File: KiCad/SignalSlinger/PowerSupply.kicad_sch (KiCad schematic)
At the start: 44 parts, among them J201 Barrel_Jack_Switch, J203 External Fan Power, J204 Controlled Power, U201 LP2985-3.3, U202 LP2985-3.3, U203 TPS63060, U204 TPS22810DBVT, U205 uA7805

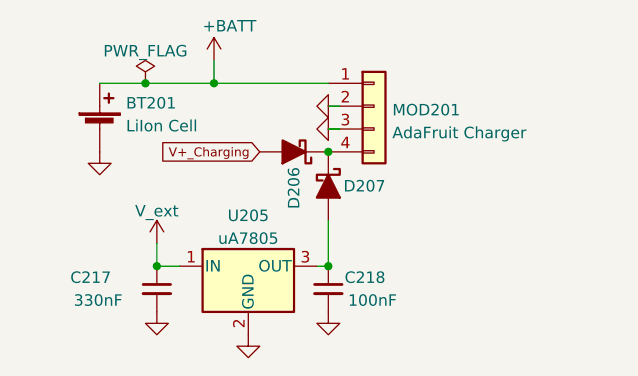
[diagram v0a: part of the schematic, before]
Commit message: Rev 2.3
Updates from initial PCB build.
Added thermal fuse F101
Support for regulated voltage
Support for charging LiPo via transmitter external power source
Updated BOM
Updated PCB and schematic
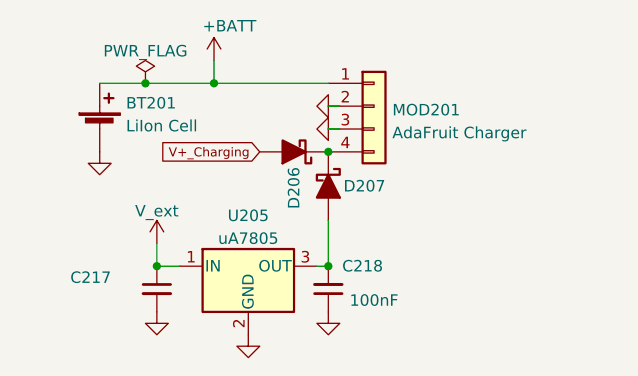
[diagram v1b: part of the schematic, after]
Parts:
- C217: value 330nF -> (none); footprint Capacitor_SMD:C_0805_2012Metric -> (none); Digi-Key Part No. 399-C0805C103J5GEC7800CT-ND -> 478-9924-1-ND; LCSC Part Number C3887673 -> C342818; Link https://www.digikey.com/short/qd893213 -> https://www.digikey.com/products/en?keywords=478-9924-1-ND; Manufacturer KEMET -> AVX Corporation; Manufacturer PN C0805C103J5GEC7800 -> 08051C474K4Z2A
- C218: Digi-Key Part No. 399-C0805C103J5GEC7800CT-ND -> 1276-1099-1-ND; LCSC Part Number C3887673 -> C29926; Link https://www.digikey.com/short/qd893213 -> https://www.digikey.com/short/q2f22qnq; Manufacturer KEMET -> Samsung Electro-Mechanics; Manufacturer PN C0805C103J5GEC7800 -> CL21B104KACNNNC
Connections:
- net GND: now also C218.1; no longer C218.2
- net at D207.2 (A), U205.3 (OUT): now also C218.2; no longer C218.1
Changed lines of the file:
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@@
   (title_block
     (title "SignalSlinger")
-    (date "2023-12-10")
-    (rev "2.2")
+    (date "2024-04-13")
+    (rev "2.3")
   )
   (junction (at 187.96 116.84) (diameter 0) (color 0 0 0 0)
@@
   (junction (at 189.23 41.91) (diameter 0) (color 0 0 0 0)
   )
+  (junction (at 55.88 170.18) (diameter 0) (color 0 0 0 0)
+  )
   (junction (at 229.87 41.91) (diameter 0) (color 0 0 0 0)
   )
@@
   )
   (junction (at 217.17 41.91) (diameter 0) (color 0 0 0 0)
-  )
-  (junction (at 55.88 170.18) (diameter 0) (color 0 0 0 0)
   )
   (junction (at 190.5 116.84) (diameter 0) (color 0 0 0 0)
@@
   (symbol (lib_id "power:+VSW") (at 107.95 46.99 0) (mirror y) (unit 1)
     (in_bom yes) (on_board yes)
-    (property "Reference" "#PWR?" (id 0) (at 107.95 50.8 0)
+    (property "Reference" "#PWR0153" (id 0) (at 107.95 50.8 0)
       (effects (font (size 1.27 1.27)) hide)
     )
@@
       (effects (font (size 1.27 1.27)) (justify left))
     )
-    (property "Value" "330nF" (id 1) (at 33.02 173.99 0)
-      (effects (font (size 1.27 1.27)) (justify left))
-    )
-    (property "Footprint" "Capacitor_SMD:C_0805_2012Metric" (id 2) (at 36.83 172.72 0)
+    (property "Value" "" (id 1) (at 33.02 173.99 0)
+      (effects (font (size 1.27 1.27)) (justify left))
+    )
+    (property "Footprint" "" (id 2) (at 36.83 172.72 0)
       (effects (font (size 1.27 1.27)) hide)
     )
@@
       (effects (font (size 1.27 1.27)) hide)
     )
-    (property "Digi-Key Part No." "399-C0805C103J5GEC7800CT-ND" (id 4) (at 36.83 172.72 0)
-      (effects (font (size 1.27 1.27)) hide)
-    )
-    (property "Manufacturer" "KEMET" (id 5) (at 36.83 172.72 0)
-      (effects (font (size 1.27 1.27)) hide)
-    )
-    (property "Manufacturer PN" "C0805C103J5GEC7800" (id 6) (at 36.83 172.72 0)
-      (effects (font (size 1.27 1.27)) hide)
-    )
-    (property "Description" "CAP CER 0805 10NF 50V C0G 5%" (id 7) (at 36.83 172.72 0)
-      (effects (font (size 1.27 1.27)) hide)
-    )
-    (property "Link" "https://www.digikey.com/short/qd893213" (id 8) (at 36.83 172.72 0)
-      (effects (font (size 1.27 1.27)) hide)
-    )
-    (property "LCSC Part Number" "C3887673" (id 9) (at 36.83 172.72 0)
+    (property "Digi-Key Part No." "478-9924-1-ND" (id 4) (at 36.83 172.72 0)
+      (effects (font (size 1.27 1.27)) hide)
+    )
+    (property "Manufacturer" "AVX Corporation" (id 5) (at 36.83 172.72 0)
+      (effects (font (size 1.27 1.27)) hide)
+    )
+    (property "Manufacturer PN" "08051C474K4Z2A" (id 6) (at 36.83 172.72 0)
+      (effects (font (size 1.27 1.27)) hide)
+    )
+    (property "Description" "CAP CER 0.47UF 100V X7R 0805" (id 7) (at 36.83 172.72 0)
+      (effects (font (size 1.27 1.27)) hide)
+    )
+    (property "Link" "https://www.digikey.com/products/en?keywords=478-9924-1-ND" (id 8) (at 36.83 172.72 0)
+      (effects (font (size 1.27 1.27)) hide)
+    )
+    (property "LCSC Part Number" "C342818" (id 9) (at 36.83 172.72 0)
       (effects (font (size 1.27 1.27)) hide)
     )
@@
     (pin "2")
   )
+  (symbol (lib_id "Device:C_Small") (at 55.88 172.72 180) (unit 1)
+    (in_bom yes) (on_board yes)
+    (property "Reference" "C218" (id 0) (at 59.69 170.18 0))
+    (property "Value" "100nF" (id 1) (at 60.96 173.99 0))
+    (property "Footprint" "Capacitor_SMD:C_0805_2012Metric" (id 2) (at 55.88 172.72 0)
+      (effects (font (size 1.27 1.27)) hide)
+    )
+    (property "Datasheet" "" (id 3) (at 55.88 172.72 0)
+      (effects (font (size 1.27 1.27)) hide)
+    )
+    (property "Digi-Key Part No." "1276-1099-1-ND" (id 4) (at 55.88 172.72 0)
+      (effects (font (size 1.27 1.27)) hide)
+    )
+    (property "Manufacturer" "Samsung Electro-Mechanics" (id 5) (at 55.88 172.72 0)
+      (effects (font (size 1.27 1.27)) hide)
+    )
+    (property "Manufacturer PN" "CL21B104KACNNNC" (id 6) (at 55.88 172.72 0)
+      (effects (font (size 1.27 1.27)) hide)
+    )
+    (property "Description" "CAP CER 0.1UF 25V X7R 0805" (id 7) (at 55.88 172.72 0)
+      (effects (font (size 1.27 1.27)) hide)
+    )
+    (property "Link" "https://www.digikey.com/short/q2f22qnq" (id 8) (at 55.88 172.72 0)
+      (effects (font (size 1.27 1.27)) hide)
+    )
+    (property "LCSC Part Number" "C29926" (id 9) (at 55.88 172.72 0)
+      (effects (font (size 1.27 1.27)) hide)
+    )
+    (pin "1")
+    (pin "2")
+  )
   (symbol (lib_id "power:GND") (at 226.06 119.38 0) (unit 1)
     (in_bom yes) (on_board yes) (fields_autoplaced)
@@
       (effects (font (size 1.27 1.27)) hide)
     )
-    (pin "1")
-    (pin "2")
-  )
-  (symbol (lib_id "Device:C_Small") (at 55.88 172.72 0) (mirror y) (unit 1)
-    (in_bom yes) (on_board yes)
-    (property "Reference" "C218" (id 0) (at 62.23 171.45 0)
-      (effects (font (size 1.27 1.27)) (justify left))
-    )
-    (property "Value" "100nF" (id 1) (at 63.5 173.99 0)
-      (effects (font (size 1.27 1.27)) (justify left))
-    )
-    (property "Footprint" "Capacitor_SMD:C_0805_2012Metric" (id 2) (at 55.88 172.72 0)
-      (effects (font (size 1.27 1.27)) hide)
-    )
-    (property "Datasheet" "" (id 3) (at 55.88 172.72 0)
-      (effects (font (size 1.27 1.27)) hide)
-    )
-    (property "Digi-Key Part No." "399-C0805C103J5GEC7800CT-ND" (id 4) (at 55.88 172.72 0)
-      (effects (font (size 1.27 1.27)) hide)
-    )
-    (property "Manufacturer" "KEMET" (id 5) (at 55.88 172.72 0)
-      (effects (font (size 1.27 1.27)) hide)
-    )
-    (property "Manufacturer PN" "C0805C103J5GEC7800" (id 6) (at 55.88 172.72 0)
-      (effects (font (size 1.27 1.27)) hide)
-    )
-    (property "Description" "CAP CER 0805 10NF 50V C0G 5%" (id 7) (at 55.88 172.72 0)
-      (effects (font (size 1.27 1.27)) hide)
-    )
-    (property "Link" "https://www.digikey.com/short/qd893213" (id 8) (at 55.88 172.72 0)
-      (effects (font (size 1.27 1.27)) hide)
-    )
-    (property "LCSC Part Number" "C3887673" (id 9) (at 55.88 172.72 0)
-      (effects (font (size 1.27 1.27)) hide)
-    )

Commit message: Ver 2.3
Updates to BOM information.
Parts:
- C213, C214, C215: value 22uF -> (none); footprint Capacitor_SMD:C_0805_2012Metric -> (none); Digi-Key Part No. 1276-3373-1-ND -> 1276-6780-1-ND; LCSC Part Number C337455 -> (none); Link https://www.digikey.com/products/en?keywords=1276-3373-1-ND -> (none); Manufacturer PN CL32A226MAJNNNE -> CL21A226MOCLRNC
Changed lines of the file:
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@@
     (pin "3")
-  )
-  (symbol (lib_id "Device:C_Small") (at 203.2 63.5 180) (unit 1)
-    (in_bom yes) (on_board yes)
-    (property "Reference" "C213" (id 0) (at 210.82 62.23 0)
-      (effects (font (size 1.27 1.27)) (justify left))
-    )
-    (property "Value" "22uF" (id 1) (at 210.82 64.77 0)
-      (effects (font (size 1.27 1.27)) (justify left))
-    )
-    (property "Footprint" "Capacitor_SMD:C_0805_2012Metric" (id 2) (at 203.2 63.5 0)
-      (effects (font (size 1.27 1.27)) hide)
-    )
-    (property "Datasheet" "" (id 3) (at 203.2 63.5 0)
-      (effects (font (size 1.27 1.27)) hide)
-    )
-    (property "Digi-Key Part No." "1276-3373-1-ND" (id 4) (at 203.2 63.5 0)
-      (effects (font (size 1.27 1.27)) hide)
-    )
-    (property "Link" "https://www.digikey.com/products/en?keywords=1276-3373-1-ND" (id 5) (at 203.2 63.5 0)
-      (effects (font (size 1.524 1.524)) hide)
-    )
-    (property "Manufacturer" "Samsung Electro-Mechanics" (id 6) (at 203.2 63.5 90)
-      (effects (font (size 1.27 1.27)) hide)
-    )
-    (property "Manufacturer PN" "CL32A226MAJNNNE" (id 7) (at 203.2 63.5 90)
-      (effects (font (size 1.27 1.27)) hide)
-    )
-    (property "Description" "CAP CER 22UF 25V X5R 1210" (id 8) (at 203.2 63.5 90)
-      (effects (font (size 1.27 1.27)) hide)
-    )
-    (property "LCSC Part Number" "C337455" (id 9) (at 203.2 63.5 0)
-      (effects (font (size 1.27 1.27)) hide)
-    )
-    (pin "1")
-    (pin "2")
   )
   (symbol (lib_id "power:V_ext") (at 71.12 96.52 0) (unit 1)
@@
     (pin "1")
   )
+  (symbol (lib_id "Device:C_Small") (at 203.2 63.5 180) (unit 1)
+    (in_bom yes) (on_board yes)
+    (property "Reference" "C213" (id 0) (at 210.82 62.23 0)
+      (effects (font (size 1.27 1.27)) (justify left))
+    )
+    (property "Value" "" (id 1) (at 210.82 64.77 0)
+      (effects (font (size 1.27 1.27)) (justify left))
+    )
+    (property "Footprint" "" (id 2) (at 203.2 63.5 0)
+      (effects (font (size 1.27 1.27)) hide)
+    )
+    (property "Datasheet" "" (id 3) (at 203.2 63.5 0)
+      (effects (font (size 1.27 1.27)) hide)
+    )
+    (property "Digi-Key Part No." "1276-6780-1-ND" (id 4) (at 203.2 63.5 0)
+      (effects (font (size 1.27 1.27)) hide)
+    )
+    (property "Manufacturer" "Samsung Electro-Mechanics" (id 6) (at 203.2 63.5 90)
+      (effects (font (size 1.27 1.27)) hide)
+    )
+    (property "Manufacturer PN" "CL21A226MOCLRNC" (id 7) (at 203.2 63.5 90)
+      (effects (font (size 1.27 1.27)) hide)
+    )
+    (property "Description" "CAP CER 22UF 16V X5R 0805" (id 8) (at 203.2 63.5 90)
+      (effects (font (size 1.27 1.27)) hide)
+    )
+    (pin "1")
+    (pin "2")
+  )
   (symbol (lib_id "Device:C_Small") (at 229.87 63.5 180) (unit 1)
     (in_bom yes) (on_board yes)
@@
       (effects (font (size 1.27 1.27)) (justify left))
     )
-    (property "Value" "22uF" (id 1) (at 237.49 64.77 0)
-      (effects (font (size 1.27 1.27)) (justify left))
-    )
-    (property "Footprint" "Capacitor_SMD:C_0805_2012Metric" (id 2) (at 229.87 63.5 0)
+    (property "Value" "" (id 1) (at 237.49 64.77 0)
+      (effects (font (size 1.27 1.27)) (justify left))
+    )
+    (property "Footprint" "" (id 2) (at 229.87 63.5 0)
       (effects (font (size 1.27 1.27)) hide)
     )
@@
       (effects (font (size 1.27 1.27)) hide)
     )
-    (property "Digi-Key Part No." "1276-3373-1-ND" (id 4) (at 229.87 63.5 0)
-      (effects (font (size 1.27 1.27)) hide)
-    )
-    (property "Link" "https://www.digikey.com/products/en?keywords=1276-3373-1-ND" (id 5) (at 229.87 63.5 0)
-      (effects (font (size 1.524 1.524)) hide)
+    (property "Digi-Key Part No." "1276-6780-1-ND" (id 4) (at 229.87 63.5 0)
+      (effects (font (size 1.27 1.27)) hide)
     )
     (property "Manufacturer" "Samsung Electro-Mechanics" (id 6) (at 229.87 63.5 90)
       (effects (font (size 1.27 1.27)) hide)
     )
-    (property "Manufacturer PN" "CL32A226MAJNNNE" (id 7) (at 229.87 63.5 90)
-      (effects (font (size 1.27 1.27)) hide)
-    )
-    (property "Description" "CAP CER 22UF 25V X5R 1210" (id 8) (at 229.87 63.5 90)
-      (effects (font (size 1.27 1.27)) hide)
-    )
-    (property "LCSC Part Number" "C337455" (id 9) (at 229.87 63.5 0)
+    (property "Manufacturer PN" "CL21A226MOCLRNC" (id 7) (at 229.87 63.5 90)
+      (effects (font (size 1.27 1.27)) hide)
+    )
+    (property "Description" "CAP CER 22UF 16V X5R 0805" (id 8) (at 229.87 63.5 90)
       (effects (font (size 1.27 1.27)) hide)
     )
@@
     )
     (property "LCSC Part Number" "C3887673" (id 9) (at 31.75 121.92 0)
+      (effects (font (size 1.27 1.27)) hide)
+    )
+    (pin "1")
+    (pin "2")
+  )
+  (symbol (lib_id "Device:C_Small") (at 217.17 63.5 180) (unit 1)
+    (in_bom yes) (on_board yes)
+    (property "Reference" "C214" (id 0) (at 224.79 62.23 0)
+      (effects (font (size 1.27 1.27)) (justify left))
+    )
+    (property "Value" "" (id 1) (at 224.79 64.77 0)
+      (effects (font (size 1.27 1.27)) (justify left))
+    )
+    (property "Footprint" "" (id 2) (at 217.17 63.5 0)
+      (effects (font (size 1.27 1.27)) hide)
+    )
+    (property "Datasheet" "" (id 3) (at 217.17 63.5 0)
+      (effects (font (size 1.27 1.27)) hide)
+    )
+    (property "Digi-Key Part No." "1276-6780-1-ND" (id 4) (at 217.17 63.5 0)
+      (effects (font (size 1.27 1.27)) hide)
+    )
+    (property "Manufacturer" "Samsung Electro-Mechanics" (id 6) (at 217.17 63.5 90)
+      (effects (font (size 1.27 1.27)) hide)
+    )
+    (property "Manufacturer PN" "CL21A226MOCLRNC" (id 7) (at 217.17 63.5 90)
+      (effects (font (size 1.27 1.27)) hide)
+    )
+    (property "Description" "CAP CER 22UF 16V X5R 0805" (id 8) (at 217.17 63.5 90)
       (effects (font (size 1.27 1.27)) hide)
     )
@@
     (pin "9")
   )
-  (symbol (lib_id "Device:C_Small") (at 217.17 63.5 180) (unit 1)
-    (in_bom yes) (on_board yes)
-    (property "Reference" "C214" (id 0) (at 224.79 62.23 0)
-      (effects (font (size 1.27 1.27)) (justify left))
-    )
-    (property "Value" "22uF" (id 1) (at 224.79 64.77 0)
-      (effects (font (size 1.27 1.27)) (justify left))
-    )
-    (property "Footprint" "Capacitor_SMD:C_0805_2012Metric" (id 2) (at 217.17 63.5 0)
-      (effects (font (size 1.27 1.27)) hide)
-    )
-    (property "Datasheet" "" (id 3) (at 217.17 63.5 0)
-      (effects (font (size 1.27 1.27)) hide)
-    )
-    (property "Digi-Key Part No." "1276-3373-1-ND" (id 4) (at 217.17 63.5 0)
-      (effects (font (size 1.27 1.27)) hide)
-    )
-    (property "Link" "https://www.digikey.com/products/en?keywords=1276-3373-1-ND" (id 5) (at 217.17 63.5 0)
-      (effects (font (size 1.524 1.524)) hide)
-    )
-    (property "Manufacturer" "Samsung Electro-Mechanics" (id 6) (at 217.17 63.5 90)
-      (effects (font (size 1.27 1.27)) hide)
-    )
-    (property "Manufacturer PN" "CL32A226MAJNNNE" (id 7) (at 217.17 63.5 90)
-      (effects (font (size 1.27 1.27)) hide)
-    )
-    (property "Description" "CAP CER 22UF 25V X5R 1210" (id 8) (at 217.17 63.5 90)
-      (effects (font (size 1.27 1.27)) hide)
-    )
-    (property "LCSC Part Number" "C337455" (id 9) (at 217.17 63.5 0)
-      (effects (font (size 1.27 1.27)) hide)
-    )
-    (pin "1")
-    (pin "2")
-  )
   (symbol (lib_id "Regulator_Linear:LP2985-3.3") (at 44.45 118.11 0) (mirror y) (unit 1)

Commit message: Ver 2.4
Minor schematic update.
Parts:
- C213, C214, C215: value (none) -> 22uF; footprint (none) -> Capacitor_SMD:C_0805_2012Metric
- C217: value (none) -> 470nF; footprint (none) -> Capacitor_SMD:C_0805_2012Metric
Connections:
- net GND: now also C218.2; no longer C218.1
- net at D207.2 (A), U205.3 (OUT): now also C218.1; no longer C218.2
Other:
- moved on the sheet: C218
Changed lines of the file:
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@@
   (title_block
     (title "SignalSlinger")
-    (date "2024-04-13")
-    (rev "2.3")
+    (date "2024-04-15")
+    (rev "2.4")
   )
   (junction (at 187.96 116.84) (diameter 0) (color 0 0 0 0)
@@
   (junction (at 189.23 41.91) (diameter 0) (color 0 0 0 0)
   )
+  (junction (at 229.87 41.91) (diameter 0) (color 0 0 0 0)
+  )
+  (junction (at 73.66 109.22) (diameter 0) (color 0 0 0 0)
+  )
+  (junction (at 73.66 33.02) (diameter 0) (color 0 0 0 0)
+  )
+  (junction (at 93.98 46.99) (diameter 0) (color 0 0 0 0)
+  )
+  (junction (at 100.33 54.61) (diameter 0) (color 0 0 0 0)
+  )
+  (junction (at 203.2 41.91) (diameter 0) (color 0 0 0 0)
+  )
+  (junction (at 114.3 114.3) (diameter 0) (color 0 0 0 0)
+  )
+  (junction (at 87.63 109.22) (diameter 0) (color 0 0 0 0)
+  )
+  (junction (at 35.56 149.86) (diameter 0) (color 0 0 0 0)
+  )
+  (junction (at 119.38 54.61) (diameter 0) (color 0 0 0 0)
+  )
+  (junction (at 36.83 170.18) (diameter 0) (color 0 0 0 0)
+  )
+  (junction (at 54.61 115.57) (diameter 0) (color 0 0 0 0)
+  )
+  (junction (at 163.83 64.77) (diameter 0) (color 0 0 0 0)
+  )
+  (junction (at 163.83 54.61) (diameter 0) (color 0 0 0 0)
+  )
+  (junction (at 217.17 41.91) (diameter 0) (color 0 0 0 0)
+  )
+  (junction (at 190.5 116.84) (diameter 0) (color 0 0 0 0)
+  )
+  (junction (at 80.01 33.02) (diameter 0) (color 0 0 0 0)
+  )
+  (junction (at 118.11 57.15) (diameter 0) (color 0 0 0 0)
+  )
+  (junction (at 43.18 149.86) (diameter 0) (color 0 0 0 0)
+  )
+  (junction (at 57.15 113.03) (diameter 0) (color 0 0 0 0)
+  )
+  (junction (at 30.48 115.57) (diameter 0) (color 0 0 0 0)
+  )
   (junction (at 55.88 170.18) (diameter 0) (color 0 0 0 0)
-  )
-  (junction (at 229.87 41.91) (diameter 0) (color 0 0 0 0)
-  )
-  (junction (at 73.66 109.22) (diameter 0) (color 0 0 0 0)
-  )
-  (junction (at 73.66 33.02) (diameter 0) (color 0 0 0 0)
-  )
-  (junction (at 93.98 46.99) (diameter 0) (color 0 0 0 0)
-  )
-  (junction (at 100.33 54.61) (diameter 0) (color 0 0 0 0)
-  )
-  (junction (at 203.2 41.91) (diameter 0) (color 0 0 0 0)
-  )
-  (junction (at 114.3 114.3) (diameter 0) (color 0 0 0 0)
-  )
-  (junction (at 87.63 109.22) (diameter 0) (color 0 0 0 0)
-  )
-  (junction (at 35.56 149.86) (diameter 0) (color 0 0 0 0)
-  )
-  (junction (at 119.38 54.61) (diameter 0) (color 0 0 0 0)
-  )
-  (junction (at 36.83 170.18) (diameter 0) (color 0 0 0 0)
-  )
-  (junction (at 54.61 115.57) (diameter 0) (color 0 0 0 0)
-  )
-  (junction (at 163.83 64.77) (diameter 0) (color 0 0 0 0)
-  )
-  (junction (at 163.83 54.61) (diameter 0) (color 0 0 0 0)
-  )
-  (junction (at 217.17 41.91) (diameter 0) (color 0 0 0 0)
-  )
-  (junction (at 190.5 116.84) (diameter 0) (color 0 0 0 0)
-  )
-  (junction (at 80.01 33.02) (diameter 0) (color 0 0 0 0)
-  )
-  (junction (at 118.11 57.15) (diameter 0) (color 0 0 0 0)
-  )
-  (junction (at 43.18 149.86) (diameter 0) (color 0 0 0 0)
-  )
-  (junction (at 57.15 113.03) (diameter 0) (color 0 0 0 0)
-  )
-  (junction (at 30.48 115.57) (diameter 0) (color 0 0 0 0)
   )
   (junction (at 181.61 85.09) (diameter 0) (color 0 0 0 0)
@@
     (stroke (width 0) (type default) (color 0 0 0 0))
   )
+  (wire (pts (xy 54.61 170.18) (xy 55.88 170.18))
+    (stroke (width 0) (type default) (color 0 0 0 0))
+  )
   (wire (pts (xy 163.83 64.77) (xy 172.72 64.77))
     (stroke (width 0) (type default) (color 0 0 0 0))
@@
   )
   (wire (pts (xy 172.72 68.58) (xy 172.72 64.77))
-    (stroke (width 0) (type default) (color 0 0 0 0))
-  )
-  (wire (pts (xy 54.61 170.18) (xy 55.88 170.18))
     (stroke (width 0) (type default) (color 0 0 0 0))
   )
@@
       (effects (font (size 1.27 1.27)) (justify left))
     )
-    (property "Value" "" (id 1) (at 33.02 173.99 0)
-      (effects (font (size 1.27 1.27)) (justify left))
-    )
-    (property "Footprint" "" (id 2) (at 36.83 172.72 0)
+    (property "Value" "470nF" (id 1) (at 33.02 173.99 0)
+      (effects (font (size 1.27 1.27)) (justify left))
+    )
+    (property "Footprint" "Capacitor_SMD:C_0805_2012Metric" (id 2) (at 36.83 172.72 0)
       (effects (font (size 1.27 1.27)) hide)
     )
@@
       (effects (font (size 1.27 1.27)) (justify left))
     )
-    (property "Value" "" (id 1) (at 210.82 64.77 0)
-      (effects (font (size 1.27 1.27)) (justify left))
-    )
-    (property "Footprint" "" (id 2) (at 203.2 63.5 0)
+    (property "Value" "22uF" (id 1) (at 210.82 64.77 0)
+      (effects (font (size 1.27 1.27)) (justify left))
+    )
+    (property "Footprint" "Capacitor_SMD:C_0805_2012Metric" (id 2) (at 203.2 63.5 0)
       (effects (font (size 1.27 1.27)) hide)
     )
@@
       (effects (font (size 1.27 1.27)) (justify left))
     )
-    (property "Value" "" (id 1) (at 237.49 64.77 0)
-      (effects (font (size 1.27 1.27)) (justify left))
-    )
-    (property "Footprint" "" (id 2) (at 229.87 63.5 0)
+    (property "Value" "22uF" (id 1) (at 237.49 64.77 0)
+      (effects (font (size 1.27 1.27)) (justify left))
+    )
+    (property "Footprint" "Capacitor_SMD:C_0805_2012Metric" (id 2) (at 229.87 63.5 0)
       (effects (font (size 1.27 1.27)) hide)
     )
@@
     (pin "2")
   )
-  (symbol (lib_id "Device:C_Small") (at 55.88 172.72 180) (unit 1)
-    (in_bom yes) (on_board yes)
-    (property "Reference" "C218" (id 0) (at 59.69 170.18 0))
-    (property "Value" "100nF" (id 1) (at 60.96 173.99 0))
+  (symbol (lib_id "Device:C_Small") (at 55.88 172.72 0) (unit 1)
+    (in_bom yes) (on_board yes)
+    (property "Reference" "C218" (id 0) (at 59.69 175.26 0))
+    (property "Value" "100nF" (id 1) (at 60.96 171.45 0))
     (property "Footprint" "Capacitor_SMD:C_0805_2012Metric" (id 2) (at 55.88 172.72 0)
       (effects (font (size 1.27 1.27)) hide)
@@
       (effects (font (size 1.27 1.27)) (justify left))
     )
-    (property "Value" "" (id 1) (at 224.79 64.77 0)
-      (effects (font (size 1.27 1.27)) (justify left))
-    )
-    (property "Footprint" "" (id 2) (at 217.17 63.5 0)
-      (effects (font (size 1.27 1.27)) hide)
-    )
+    (property "Value" "22uF" (id 1) (at 224.79 64.77 0)
+      (effects (font (size 1.27 1.27)) (justify left))
+    )
+    (property "Footprint" "Capacitor_SMD:C_0805_2012Metric" (id 2) (at 217.17 63.5 0)
+      (effects (font (size 1.27 1.27)) hide)
+    )
